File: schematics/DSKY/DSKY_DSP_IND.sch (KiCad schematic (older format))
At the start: 93 parts, among them Q1 Q_NPN, Q10 Q_NPN, Q11 Q_NPN, Q12 Q_NPN, Q13 Q_NPN, Q14 Q_NPN, Q15 Q_NPN, Q16 Q_NPN, Q3 Q_NPN, Q4 Q_NPN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

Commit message: Add files via upload
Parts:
- removed D1, D2: LED, symbol Device:LED
- removed Q1: Q_NPN, symbol Device:Q_NPN_BCE
- removed R12, R13: 220, symbol Device:R_US
- removed R4: 1k, symbol Device:R_US
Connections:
- net STBY: now also U42.11; no longer U42.3
- net at R32.1: now also U42.10; no longer U42.4
- no-connect marks 1 -> 2
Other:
- note removed: "PRIO DISP"
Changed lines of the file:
@@
 	7000 3200 7300 3200
-Wire Wire Line
-	7100 1550 7750 1550
-Wire Wire Line
-	7100 3000 7100 1550
-Wire Wire Line
-	7000 3000 7100 3000
 Wire Wire Line
 	10200 4450 10200 4850
@@
 Wire Wire Line
 	9950 2300 10200 2300
-Connection ~ 10200 1950
 Wire Wire Line
 	9950 1950 10200 1950
@@
 F 3 "~" H 8450 2300 50  0001 C CNN
 	1    8450 2300
-	1    0    0    -1
-$EndComp
-Text Notes 10450 1400 2    50   ~ 0
-Green
-Text Notes 7750 1500 2    50   ~ 0
-PRIO DISP
-Wire Wire Line
-	9050 1350 9050 1550
-Connection ~ 9050 1350
-Wire Wire Line
-	8550 1350 9050 1350
-Wire Wire Line
-	9050 1550 9200 1550
-Wire Wire Line
-	9050 1200 9050 1350
-Wire Wire Line
-	9200 1200 9050 1200
-Wire Wire Line
-	8050 1550 8250 1550
-Wire Wire Line
-	9950 1550 10200 1550
-Wire Wire Line
-	9950 1200 10200 1200
-$Comp
-L power:+5V #PWR0120
-U 1 1 68A945F4
-P 10200 1050
-F 0 "#PWR0120" H 10200 900 50  0001 C CNN
-F 1 "+5V" H 10215 1223 50  0000 C CNN
-F 2 "" H 10200 1050 50  0001 C CNN
-F 3 "" H 10200 1050 50  0001 C CNN
-	1    10200 1050
-	1    0    0    -1
-$EndComp
-Wire Wire Line
-	9650 1200 9500 1200
-Wire Wire Line
-	9650 1550 9500 1550
-$Comp
-L power:GND #PWR0118
-U 1 1 68A945E4
-P 8550 1750
-F 0 "#PWR0118" H 8550 1500 50  0001 C CNN
-F 1 "GND" H 8555 1577 50  0000 C CNN
-F 2 "" H 8550 1750 50  0001 C CNN
-F 3 "" H 8550 1750 50  0001 C CNN
-	1    8550 1750
-	1    0    0    -1
-$EndComp
-$Comp
-L Device:R_US R13
-U 1 1 68A945D2
-P 9800 1550
-F 0 "R13" V 10005 1550 50  0000 C CNN
-F 1 "220" V 9914 1550 50  0000 C CNN
-F 2 "" V 9840 1540 50  0001 C CNN
-F 3 "~" H 9800 1550 50  0001 C CNN
-	1    9800 1550
-	0    -1   -1   0
-$EndComp
-$Comp
-L Device:R_US R12
-U 1 1 68A945CC
-P 9800 1200
-F 0 "R12" V 10005 1200 50  0000 C CNN
-F 1 "220" V 9914 1200 50  0000 C CNN
-F 2 "" V 9840 1190 50  0001 C CNN
-F 3 "~" H 9800 1200 50  0001 C CNN
-	1    9800 1200
-	0    -1   -1   0
-$EndComp
-$Comp
-L Device:LED D1
-U 1 1 68A945BA
-P 9350 1200
-F 0 "D1" H 9343 1417 50  0000 C CNN
-F 1 "LED" H 9343 1326 50  0000 C CNN
-F 2 "" H 9350 1200 50  0001 C CNN
-F 3 "~" H 9350 1200 50  0001 C CNN
-	1    9350 1200
-	1    0    0    -1
-$EndComp
-$Comp
-L Device:LED D2
-U 1 1 68A945B4
-P 9350 1550
-F 0 "D2" H 9343 1767 50  0000 C CNN
-F 1 "LED" H 9343 1676 50  0000 C CNN
-F 2 "" H 9350 1550 50  0001 C CNN
-F 3 "~" H 9350 1550 50  0001 C CNN
-	1    9350 1550
-	1    0    0    -1
-$EndComp
-$Comp
-L Device:R_US R4
-U 1 1 68A945A8
-P 7900 1550
-F 0 "R4" V 8105 1550 50  0000 C CNN
-F 1 "1k" V 8014 1550 50  0000 C CNN
-F 2 "" V 7940 1540 50  0001 C CNN
-F 3 "~" H 7900 1550 50  0001 C CNN
-	1    7900 1550
-	0    -1   -1   0
-$EndComp
-$Comp
-L Device:Q_NPN_BCE Q1
-U 1 1 68A9459C
-P 8450 1550
-F 0 "Q1" H 8641 1596 50  0000 L CNN
-F 1 "Q_NPN" H 8641 1505 50  0000 L CNN
-F 2 "" H 8650 1650 50  0001 C CNN
-F 3 "~" H 8450 1550 50  0001 C CNN
-	1    8450 1550
 	1    0    0    -1
 $EndComp
@@
 $Comp
 L 74xx:74LS04 U?
-U 2 1 66B1B922
+U 5 1 66B1B922
 P 2050 4450
 AR Path="/60F98A64/64844A8A/66B1B922" Ref="U?"  Part="6"
-AR Path="/60F98A64/68A00B2E/66B1B922" Ref="U42"  Part="2"
+AR Path="/60F98A64/68A00B2E/66B1B922" Ref="U42"  Part="5"
 F 0 "U42" H 2050 4767 50  0000 C CNN
 F 1 "74LS04" H 2050 4676 50  0000 C CNN
 F 2 "" H 2050 4450 50  0001 C CNN
 F 3 "http://www.ti.com/lit/gpn/sn74LS04" H 2050 4450 50  0001 C CNN
-	2    2050 4450
+	5    2050 4450
 	1    0    0    -1
 $EndComp
@@
 L power:+5V #PWR?
 U 1 1 66B1B962
-P 5000 1150
+P 10200 1800
 AR Path="/60F98A64/64844A8A/66B1B962" Ref="#PWR?"  Part="1"
 AR Path="/60F98A64/68A00B2E/66B1B962" Ref="#PWR0188"  Part="1"
-F 0 "#PWR0188" H 5000 1000 50  0001 C CNN
-F 1 "+5V" H 5015 1323 50  0000 C CNN
-F 2 "" H 5000 1150 50  0001 C CNN
-F 3 "" H 5000 1150 50  0001 C CNN
-	1    5000 1150
+F 0 "#PWR0188" H 10200 1650 50  0001 C CNN
+F 1 "+5V" H 10215 1973 50  0000 C CNN
+F 2 "" H 10200 1800 50  0001 C CNN
+F 3 "" H 10200 1800 50  0001 C CNN
+	1    10200 1800
 	1    0    0    -1
 $EndComp
 Wire Wire Line
 	4750 1300 5000 1300
-Connection ~ 5000 1300
-Wire Wire Line
-	5000 1300 5000 1150
+Wire Wire Line
+	10200 1950 10200 1800
 Wire Wire Line
 	4750 1650 5000 1650
@@
 PARALM
 Text Notes 5050 6450 0    50   ~ 0
-White
+Green
 Connection ~ 5000 5900
 Entry Wire Line
@@
 Use 9 resistor\nnetwork chips.
 NoConn ~ 7000 3100
-Connection ~ 10200 1200
-Wire Wire Line
-	10200 1200 10200 1550
-Connection ~ 10200 1550
-Wire Wire Line
-	10200 1550 10200 1950
-Wire Wire Line
-	10200 1050 10200 1200
 Wire Wire Line
 	750  3050 2550 3050
@@
 Text HLabel 7350 6150 2    50   Output ~ 0
 PROG
+NoConn ~ 7000 3000
+Connection ~ 10200 1950
+$Comp
+L power:+5V #PWR?
+U 1 1 616BC033
+P 5000 1150
+AR Path="/60F98A64/64844A8A/616BC033" Ref="#PWR?"  Part="1"
+AR Path="/60F98A64/68A00B2E/616BC033" Ref="#PWR?"  Part="1"
+F 0 "#PWR?" H 5000 1000 50  0001 C CNN
+F 1 "+5V" H 5015 1323 50  0000 C CNN
+F 2 "" H 5000 1150 50  0001 C CNN
+F 3 "" H 5000 1150 50  0001 C CNN
+	1    5000 1150
+	1    0    0    -1
+$EndComp
+Wire Wire Line
+	5000 1300 5000 1150
+Connection ~ 5000 1300
 Wire Bus Line
 	5550 3600 5550 4050

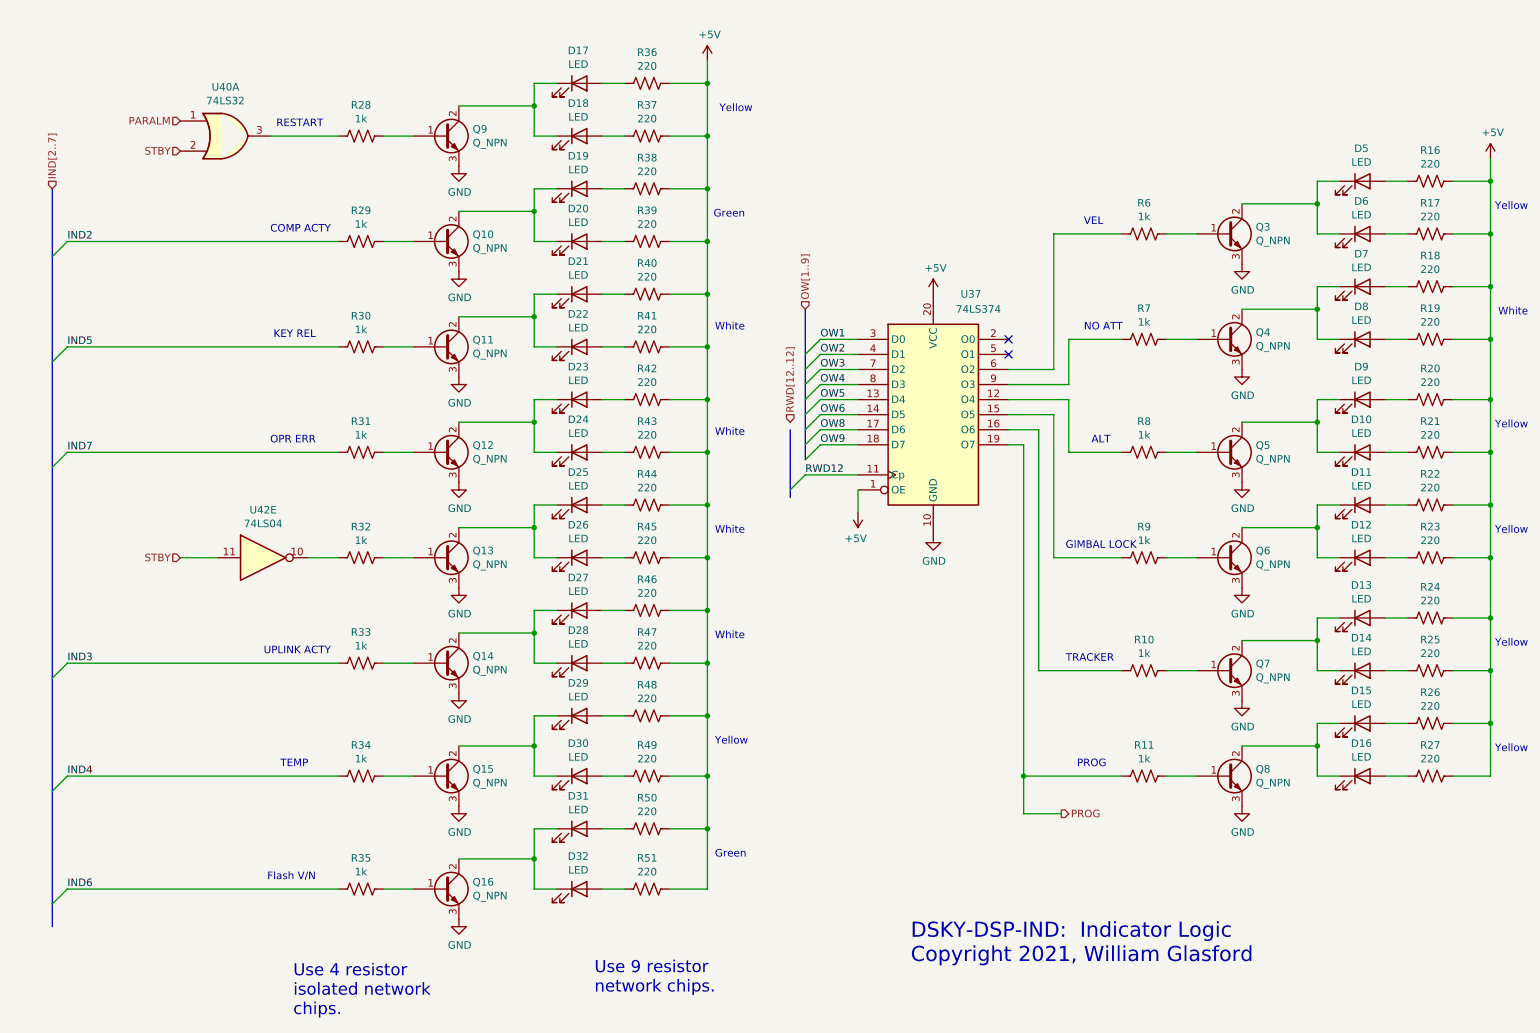
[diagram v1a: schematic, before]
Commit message: Minor tweaks to the display decoding logic.
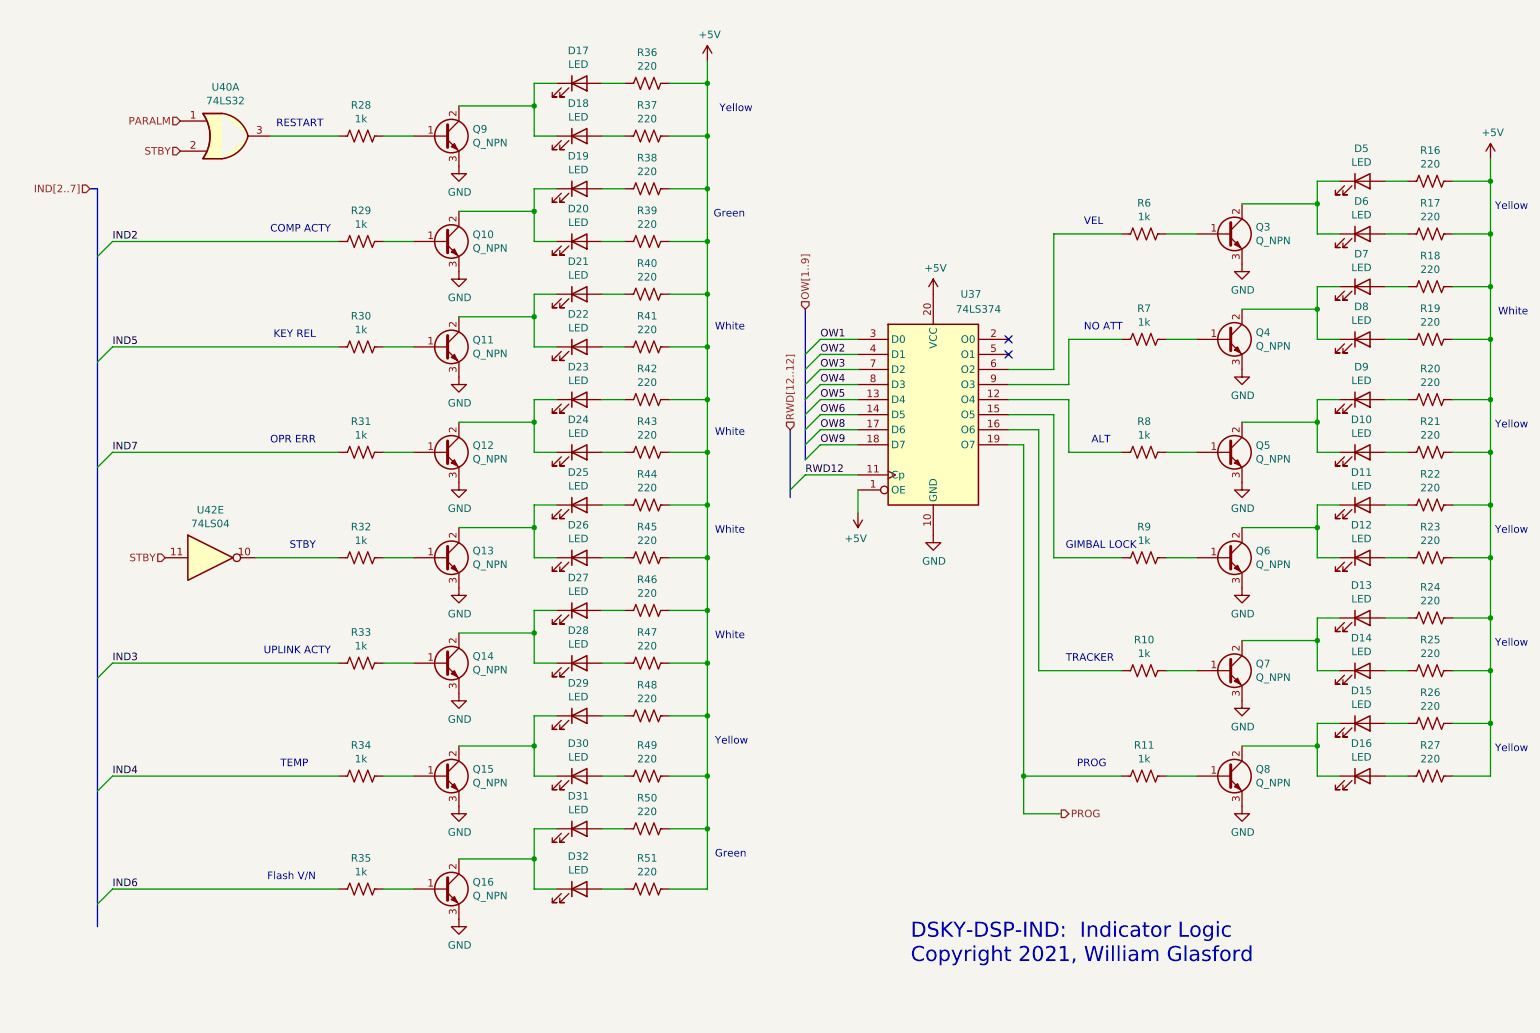
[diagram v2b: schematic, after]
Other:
- note added: "STBY"
- note removed: "Use 4 resistor\nisolated network\nchips."
- note removed: "Use 9 resistor\nnetwork chips."
- moved on the sheet: U42E
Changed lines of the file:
@@
 L 74xx:74LS04 U?
 U 5 1 66B1B922
-P 2050 4450
+P 1700 4450
 AR Path="/60F98A64/64844A8A/66B1B922" Ref="U?"  Part="6"
 AR Path="/60F98A64/68A00B2E/66B1B922" Ref="U42"  Part="5"
-F 0 "U42" H 2050 4767 50  0000 C CNN
-F 1 "74LS04" H 2050 4676 50  0000 C CNN
-F 2 "" H 2050 4450 50  0001 C CNN
-F 3 "http://www.ti.com/lit/gpn/sn74LS04" H 2050 4450 50  0001 C CNN
-	5    2050 4450
+F 0 "U42" H 1700 4767 50  0000 C CNN
+F 1 "74LS04" H 1700 4676 50  0000 C CNN
+F 2 "" H 1700 4450 50  0001 C CNN
+F 3 "http://www.ti.com/lit/gpn/sn74LS04" H 1700 4450 50  0001 C CNN
+	5    1700 4450
 	1    0    0    -1
 $EndComp
@@
 	2850 5900 3050 5900
 Wire Wire Line
-	2350 4450 2550 4450
+	2000 4450 2550 4450
 Wire Wire Line
 	4000 1300 3850 1300
@@
 	3850 3400 3850 3550
 Wire Wire Line
-	1750 4450 1500 4450
-Wire Wire Line
 	2100 1650 2550 1650
 Wire Wire Line
-	750  5150 2550 5150
-Wire Wire Line
-	750  5900 2550 5900
-Text HLabel 1500 4450 0    50   Input ~ 0
+	1050 5150 2550 5150
+Wire Wire Line
+	1050 5900 2550 5900
+Text HLabel 1400 4450 0    50   Input ~ 0
 STBY
 Text Notes 2450 1600 2    50   ~ 0
@@
 Connection ~ 5000 5900
 Entry Wire Line
-	650  3150 750  3050
-Entry Wire Line
-	650  3850 750  3750
-Text Label 750  3750 0    50   ~ 0
+	950  3150 1050 3050
+Entry Wire Line
+	950  3850 1050 3750
+Text Label 1050 3750 0    50   ~ 0
 IND7
-Text Label 750  3050 0    50   ~ 0
+Text Label 1050 3050 0    50   ~ 0
 IND5
 Entry Wire Line
-	650  2450 750  2350
-Text Label 750  2350 0    50   ~ 0
+	950  2450 1050 2350
+Text Label 1050 2350 0    50   ~ 0
 IND2
 Entry Wire Line
-	650  5250 750  5150
-Entry Wire Line
-	650  6000 750  5900
-Text Label 750  5150 0    50   ~ 0
+	950  5250 1050 5150
+Entry Wire Line
+	950  6000 1050 5900
+Text Label 1050 5150 0    50   ~ 0
 IND3
-Text Label 750  5900 0    50   ~ 0
+Text Label 1050 5900 0    50   ~ 0
 IND4
 $Comp
@@
 	1    0    0    -1
 $EndComp
-Text HLabel 650  2000 1    50   Input ~ 0
+Text HLabel 900  2000 0    50   Input ~ 0
 IND[2..7]
 Wire Wire Line
-	750  2350 2550 2350
-Text HLabel 5550 3550 1    50   Input ~ 0
+	1050 2350 2550 2350
+Text HLabel 5550 3600 1    50   Input ~ 0
 RWD[12..12]
 Wire Wire Line
@@
 Text Notes 6350 7150 0    100  ~ 0
 DSKY-DSP-IND:  Indicator Logic\nCopyright 2021, William Glasford
-Text Notes 2250 7500 0    80   ~ 0
-Use 4 resistor\nisolated network\nchips.
-Text Notes 4250 7350 0    80   ~ 0
-Use 9 resistor\nnetwork chips.
 NoConn ~ 7000 3100
 Wire Wire Line
-	750  3050 2550 3050
-Wire Wire Line
-	750  3750 2550 3750
+	1050 3050 2550 3050
+Wire Wire Line
+	1050 3750 2550 3750
 Text HLabel 1500 1750 0    50   Input ~ 0
 STBY
@@
 $EndComp
 Wire Wire Line
-	750  6650 2550 6650
-Entry Wire Line
-	650  6750 750  6650
-Text Label 750  6650 0    50   ~ 0
+	1050 6650 2550 6650
+Entry Wire Line
+	950  6750 1050 6650
+Text Label 1050 6650 0    50   ~ 0
 IND6
 Text Notes 2400 6600 2    50   ~ 0
@@
 P 5000 1150
 AR Path="/60F98A64/64844A8A/616BC033" Ref="#PWR?"  Part="1"
-AR Path="/60F98A64/68A00B2E/616BC033" Ref="#PWR?"  Part="1"
-F 0 "#PWR?" H 5000 1000 50  0001 C CNN
+AR Path="/60F98A64/68A00B2E/616BC033" Ref="#PWR0104"  Part="1"
+F 0 "#PWR0104" H 5000 1000 50  0001 C CNN
 F 1 "+5V" H 5015 1323 50  0000 C CNN
 F 2 "" H 5000 1150 50  0001 C CNN
@@
 	5000 1300 5000 1150
 Connection ~ 5000 1300
+Text Notes 2400 4400 2    50   ~ 0
+STBY
+Wire Bus Line
+	950  2000 900  2000
 Wire Bus Line
 	5550 3600 5550 4050
 Wire Bus Line
-	650  2000 650  6900
+	950  2000 950  6900
 Wire Bus Line
 	5650 2800 5650 3800

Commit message: Minor tweaks.
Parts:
- removed U42: 74LS04, symbol 74xx:74LS04
- added U42: 74LS04, symbol 74xx:74LS04
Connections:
- net +5V: no longer U37.1 (OE)
- net GND: now also U37.1 (OE)
- net RWD12: now also U42.1; no longer U37.11 (Cp)
- net STBY: now also R32.1
- net OW1: no longer names the net of U37.3 (D0)
- net OW2: no longer names the net of U37.4 (D1)
- new net: U37.11 (Cp), U42.2
- no-connect marks 2 -> 4
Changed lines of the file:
@@
 Text Label 5750 3200 0    50   ~ 0
 OW3
-Text Label 5750 3100 0    50   ~ 0
-OW2
-Text Label 5750 3000 0    50   ~ 0
-OW1
 Entry Wire Line
 	5650 3800 5750 3700
@@
 Entry Wire Line
 	5650 3300 5750 3200
-Entry Wire Line
-	5650 3200 5750 3100
-Entry Wire Line
-	5650 3100 5750 3000
 Wire Wire Line
 	6000 3700 5750 3700
@@
 Wire Wire Line
 	6000 3200 5750 3200
-Wire Wire Line
-	6000 3100 5750 3100
-Wire Wire Line
-	6000 3000 5750 3000
 Text HLabel 5650 2800 1    50   Input ~ 0
-OW[1..9]
+OW[3..9]
 Wire Wire Line
 	7100 5900 7750 5900
@@
 	1    8450 2300
 	1    0    0    -1
-$EndComp
-$Comp
-L power:+5V #PWR?
-U 1 1 68A89292
-P 6000 4150
-AR Path="/60F98A64/637944C1/68A89292" Ref="#PWR?"  Part="1"
-AR Path="/60F98A64/64844A8A/68A89292" Ref="#PWR?"  Part="1"
-AR Path="/60F98A64/63794472/68A89292" Ref="#PWR?"  Part="1"
-AR Path="/60F98A64/68A00B2E/68A89292" Ref="#PWR0117"  Part="1"
-F 0 "#PWR0117" H 6000 4000 50  0001 C CNN
-F 1 "+5V" H 6015 4323 50  0000 C CNN
-F 2 "" H 6000 4150 50  0001 C CNN
-F 3 "" H 6000 4150 50  0001 C CNN
-	1    6000 4150
-	-1   0    0    1
 $EndComp
 Wire Wire Line
@@
 $EndComp
 $Comp
-L 74xx:74LS04 U?
-U 5 1 66B1B922
-P 1700 4450
-AR Path="/60F98A64/64844A8A/66B1B922" Ref="U?"  Part="6"
-AR Path="/60F98A64/68A00B2E/66B1B922" Ref="U42"  Part="5"
-F 0 "U42" H 1700 4767 50  0000 C CNN
-F 1 "74LS04" H 1700 4676 50  0000 C CNN
-F 2 "" H 1700 4450 50  0001 C CNN
-F 3 "http://www.ti.com/lit/gpn/sn74LS04" H 1700 4450 50  0001 C CNN
-	5    1700 4450
-	1    0    0    -1
-$EndComp
-$Comp
 L power:GND #PWR?
 U 1 1 66B1B928
@@
 Wire Wire Line
 	1050 5900 2550 5900
-Text HLabel 1400 4450 0    50   Input ~ 0
+Text HLabel 2000 4450 0    50   Input ~ 0
 STBY
 Text Notes 2450 1600 2    50   ~ 0
@@
 Wire Wire Line
 	1050 2350 2550 2350
-Text HLabel 5550 3600 1    50   Input ~ 0
+Text HLabel 5350 4950 1    50   Input ~ 0
 RWD[12..12]
 Wire Wire Line
-	5650 3900 6000 3900
+	5450 5250 5800 5250
 Entry Wire Line
-	5550 4000 5650 3900
-Text Label 5650 3900 0    50   ~ 0
+	5350 5350 5450 5250
+Text Label 5450 5250 0    50   ~ 0
 RWD12
 Text Notes 6350 7150 0    100  ~ 0
@@
 Wire Bus Line
 	950  2000 900  2000
+NoConn ~ 6000 3000
+NoConn ~ 6000 3100
+$Comp
+L power:GND #PWR?
+U 1 1 635E6D82
+P 6000 4150
+AR Path="/60F98A64/637944C1/635E6D82" Ref="#PWR?"  Part="1"
+AR Path="/60F98A64/64844A8A/635E6D82" Ref="#PWR?"  Part="1"
+AR Path="/60F98A64/63794472/635E6D82" Ref="#PWR?"  Part="1"
+AR Path="/60F98A64/68A00B2E/635E6D82" Ref="#PWR0110"  Part="1"
+F 0 "#PWR0110" H 6000 3900 50  0001 C CNN
+F 1 "GND" H 6005 3977 50  0000 C CNN
+F 2 "" H 6000 4150 50  0001 C CNN
+F 3 "" H 6000 4150 50  0001 C CNN
+	1    6000 4150
+	1    0    0    -1
+$EndComp
+$Comp
+L 74xx:74LS04 U42
+U 1 1 635EB464
+P 6100 5250
+F 0 "U42" H 6100 5567 50  0000 C CNN
+F 1 "74LS04" H 6100 5476 50  0000 C CNN
+F 2 "" H 6100 5250 50  0001 C CNN
+F 3 "http://www.ti.com/lit/gpn/sn74LS04" H 6100 5250 50  0001 C CNN
+	1    6100 5250
+	1    0    0    -1
+$EndComp
+Wire Wire Line
+	6000 3900 5850 3900
+Wire Wire Line
+	5850 3900 5850 4850
+Wire Wire Line
+	5850 4850 6400 4850
+Wire Wire Line
+	6400 4850 6400 5250
 Wire Bus Line
-	5550 3600 5550 4050
+	5350 4950 5350 5400
+Wire Bus Line
+	5650 2800 5650 3800
 Wire Bus Line
 	950  2000 950  6900
-Wire Bus Line
-	5650 2800 5650 3800
 $EndSCHEMATC
